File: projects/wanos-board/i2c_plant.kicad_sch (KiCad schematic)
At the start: 8 parts, among them J10 SHT31_CINEMA, J11 SHT31_SAUNA_MID, J12 SHT31_SAUNA_HIGH, J16 LCD_I2C, J9 SHT31_BATH, U5 TCA9546A

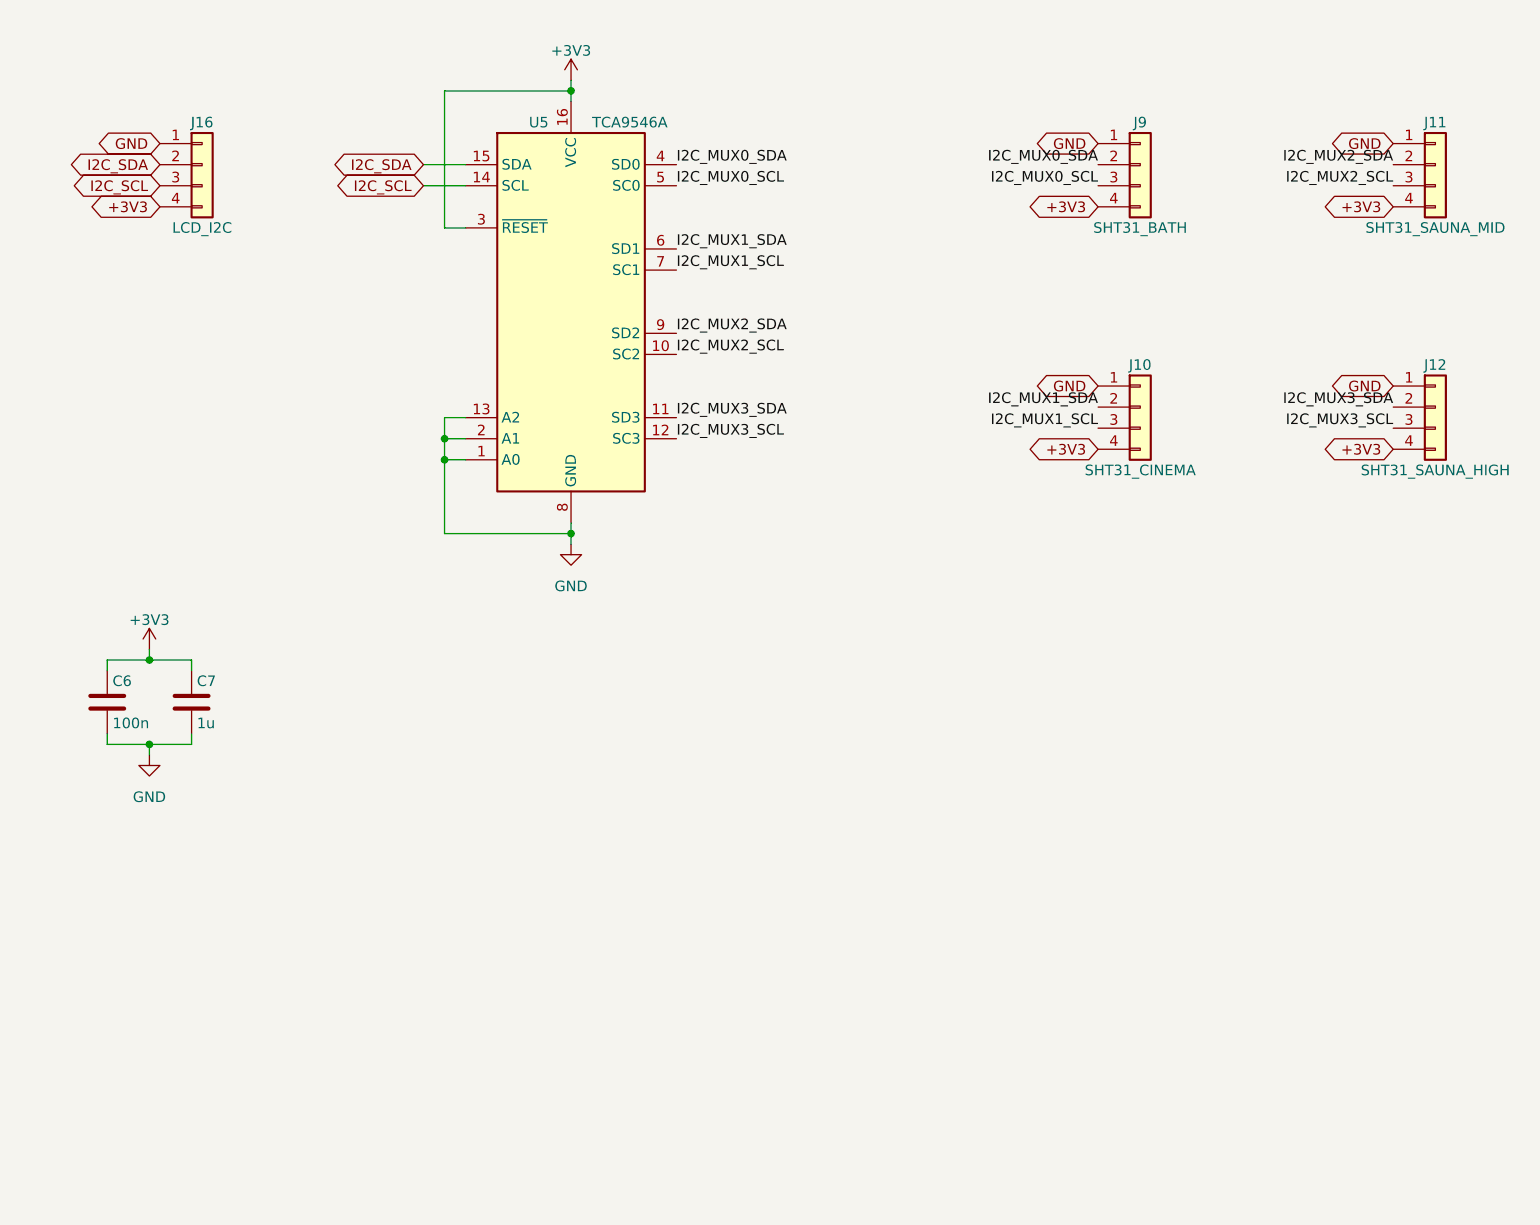
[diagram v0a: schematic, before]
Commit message: regenerate I2C sheet with 8x mux & additional SHT31
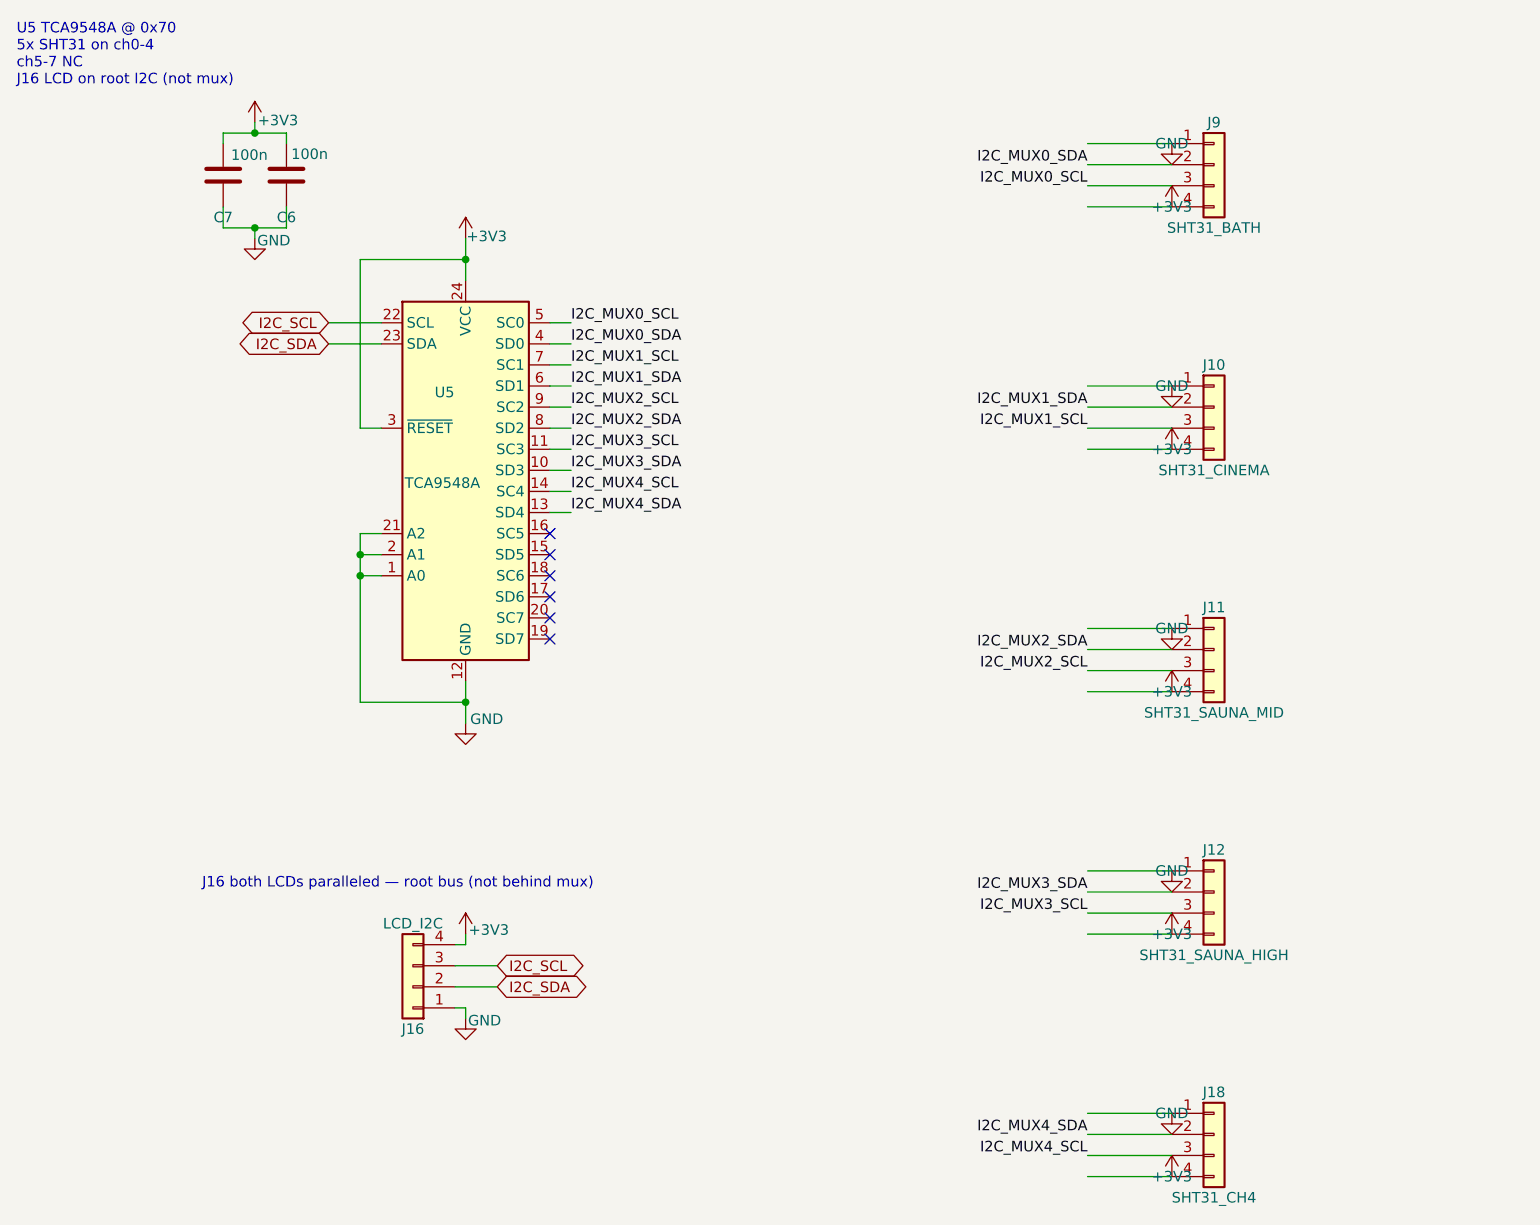
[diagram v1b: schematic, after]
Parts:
- removed U5: TCA9546A, Package_SO:TSSOP-16_4.4x5mm_P0.65mm, symbol Interface_Expansion:TCA9546APW
- added J18: SHT31_CH4, Connector_JST:JST_XH_B4B-XH-A_1x04_P2.50mm_Vertical, symbol Connector_Generic:Conn_01x04
- added U5: TCA9548A, Package_SO:TSSOP-24_4.4x7.8mm_P0.65mm, symbol Interface_Expansion:TCA9548APWR
- C7: value 1u -> 100n
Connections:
- net +3V3: now also C6.2, C7.2, J18.4 (Pin_4), U5.24 (VCC), U5.3 (~{RESET}); no longer C6.1, C7.1
- net GND: now also C6.1, C7.1, J18.1 (Pin_1), U5.1 (A0), U5.12 (GND), U5.2 (A1), U5.21 (A2); no longer C6.2, C7.2
- net I2C_MUX0_SCL: now also U5.5 (SC0)
- net I2C_MUX0_SDA: now also U5.4 (SD0)
- net I2C_MUX1_SCL: now also U5.7 (SC1)
- net I2C_MUX1_SDA: now also U5.6 (SD1)
- net I2C_MUX2_SCL: now also U5.9 (SC2)
- net I2C_MUX2_SDA: now also U5.8 (SD2)
- net I2C_MUX3_SCL: now also U5.11 (SC3)
- net I2C_MUX3_SDA: now also U5.10 (SD3)
- net I2C_SCL: now also U5.22 (SCL)
- net I2C_SDA: now also U5.23 (SDA)
- new net I2C_MUX4_SCL: J18.3 (Pin_3), U5.14 (SC4)
- new net I2C_MUX4_SDA: J18.2 (Pin_2), U5.13 (SD4)
- no-connect marks 0 -> 6
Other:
- note added: "J16 both LCDs paralleled — root bus (not behind mux)"
- note added: "U5 TCA9548A @ 0x70 5x SHT31 on ch0-4 ch5-7 NC J16 LCD on root I2C (not mux)"
- title: (none) -> wanos-pcb-v1 I2C Plant

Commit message: schema updates
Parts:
- removed C7: 100n, Capacitor_SMD:C_0805_2012Metric, symbol Device:C
- added R11: 10k, Resistor_SMD:R_0805_2012Metric, symbol Device:R
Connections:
- net +3V3: now also R11.1; no longer U5.3 (~{RESET})
- new net: R11.2, U5.3 (~{RESET})
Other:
- moved on the sheet: C6, J10, J11, J12, J18, J9
